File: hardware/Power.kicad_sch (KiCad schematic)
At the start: 40 parts, among them U2 LM2596S-12, U3 LM2596S-5, U4 LP2950-3.3_TO92

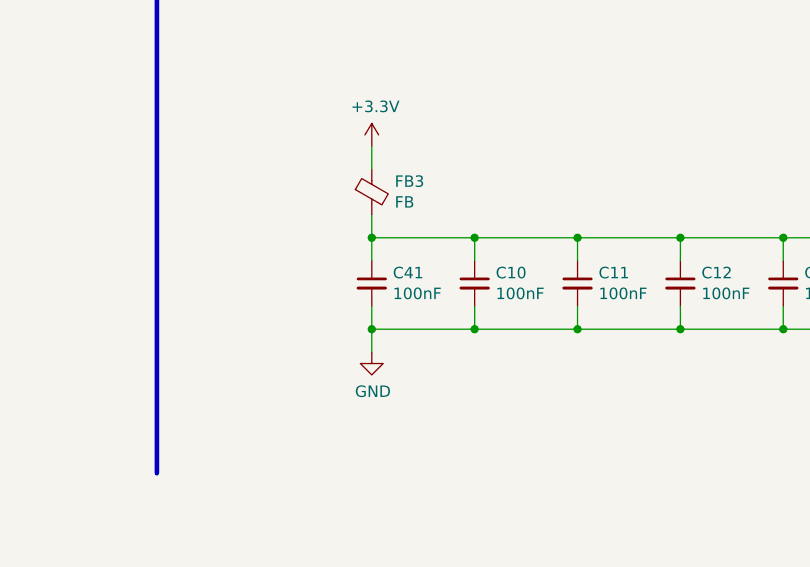
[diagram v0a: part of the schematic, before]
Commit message: changed clock and 5v converter coils, footprints rearrange commponets to fit the need now the board connector is vertical not horizontal relative to the pcb's longest side
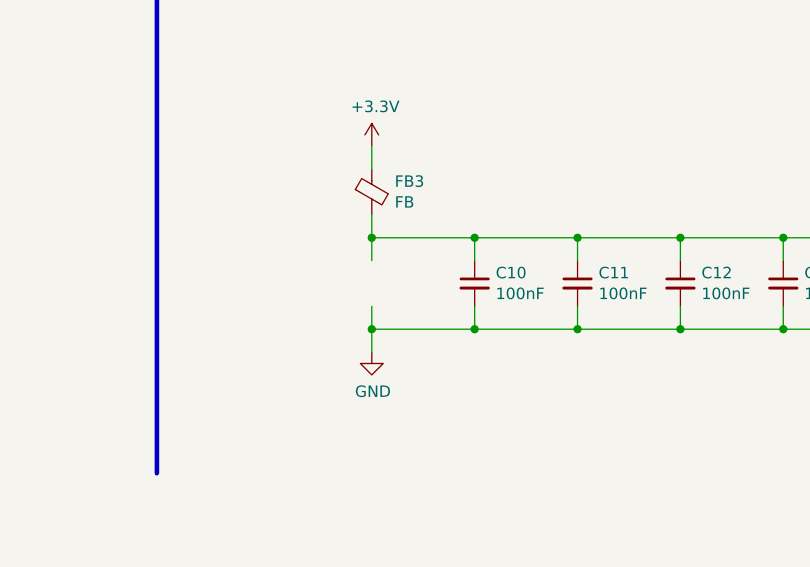
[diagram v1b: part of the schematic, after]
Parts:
- removed C41: 100nF, Capacitor_SMD:C_0603_1608Metric, symbol Device:C_Small
- L2, L4: footprint Inductor_SMD:L_12x12mm_H8mm -> Inductor_SMD:L_7.3x7.3_H4.5
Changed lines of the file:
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@@
     (property "Reference" "L4" (id 0) (at 59.69 148.844 90))
     (property "Value" "22uH" (id 1) (at 59.69 152.654 90))
-    (property "Footprint" "Inductor_SMD:L_12x12mm_H8mm" (id 2) (at 59.69 151.384 0)
+    (property "Footprint" "Inductor_SMD:L_7.3x7.3_H4.5" (id 2) (at 59.69 151.384 0)
       (effects (font (size 1.27 1.27)) hide)
     )
@@
     (pin "5")
   )
-  (symbol (lib_id "Device:C_Small") (at 200.406 145.288 0) (unit 1)
-    (in_bom yes) (on_board yes)
-    (property "Reference" "C41" (id 0) (at 202.7428 144.1196 0)
-      (effects (font (size 1.27 1.27)) (justify left))
-    )
-    (property "Value" "100nF" (id 1) (at 202.7428 146.431 0)
-      (effects (font (size 1.27 1.27)) (justify left))
-    )
-    (property "Footprint" "Capacitor_SMD:C_0603_1608Metric" (id 2) (at 200.406 145.288 0)
-      (effects (font (size 1.27 1.27)) hide)
-    )
-    (property "Datasheet" "~" (id 3) (at 200.406 145.288 0)
-      (effects (font (size 1.27 1.27)) hide)
-    )
-    (pin "1")
-    (pin "2")
-  )
   (symbol (lib_id "Device:L_Small") (at 119.38 156.464 90) (unit 1)
     (in_bom yes) (on_board yes)
     (property "Reference" "L2" (id 0) (at 119.38 153.924 90))
     (property "Value" "22uH" (id 1) (at 119.38 157.734 90))
-    (property "Footprint" "Inductor_SMD:L_12x12mm_H8mm" (id 2) (at 119.38 156.464 0)
-      (effects (font (size 1.27 1.27)) hide)
-    )
+    (property "Footprint" "Inductor_SMD:L_7.3x7.3_H4.5" (id 2) (at 119.38 156.464 0)
+      (effects (font (size 1.27 1.27)) hide)
+    )

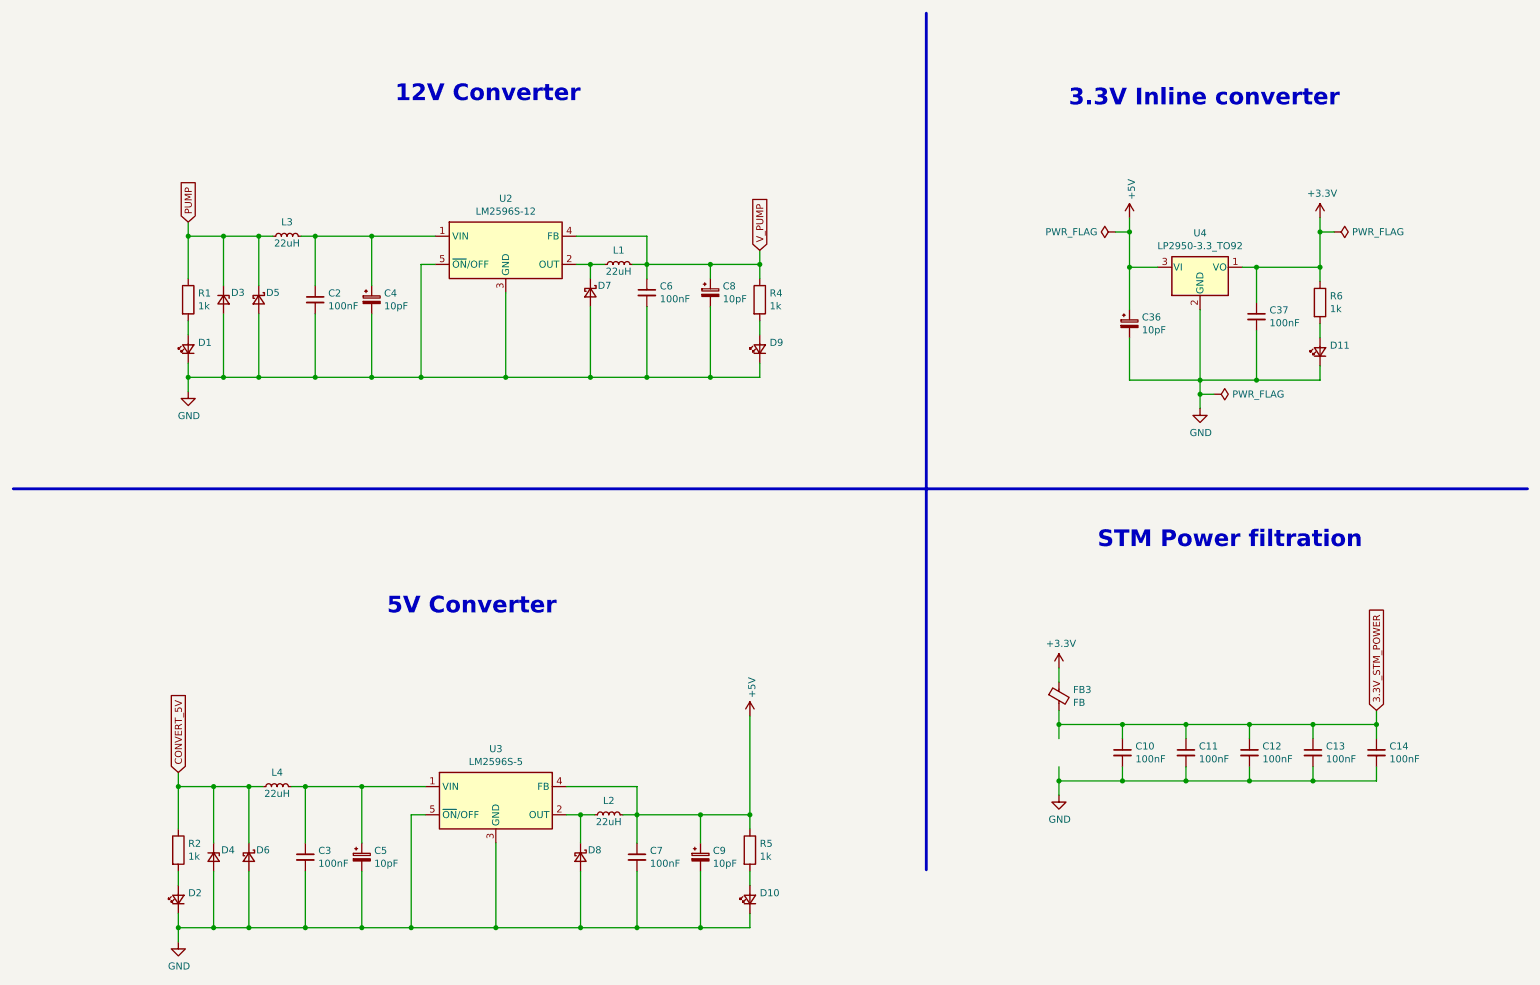
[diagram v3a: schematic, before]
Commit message: major schematic update, changed optocouplers for different, added new fuses for 5v supply for water and potentiometers and 24v supply for BSPD/ESB, updated autosport connector, and some other changes
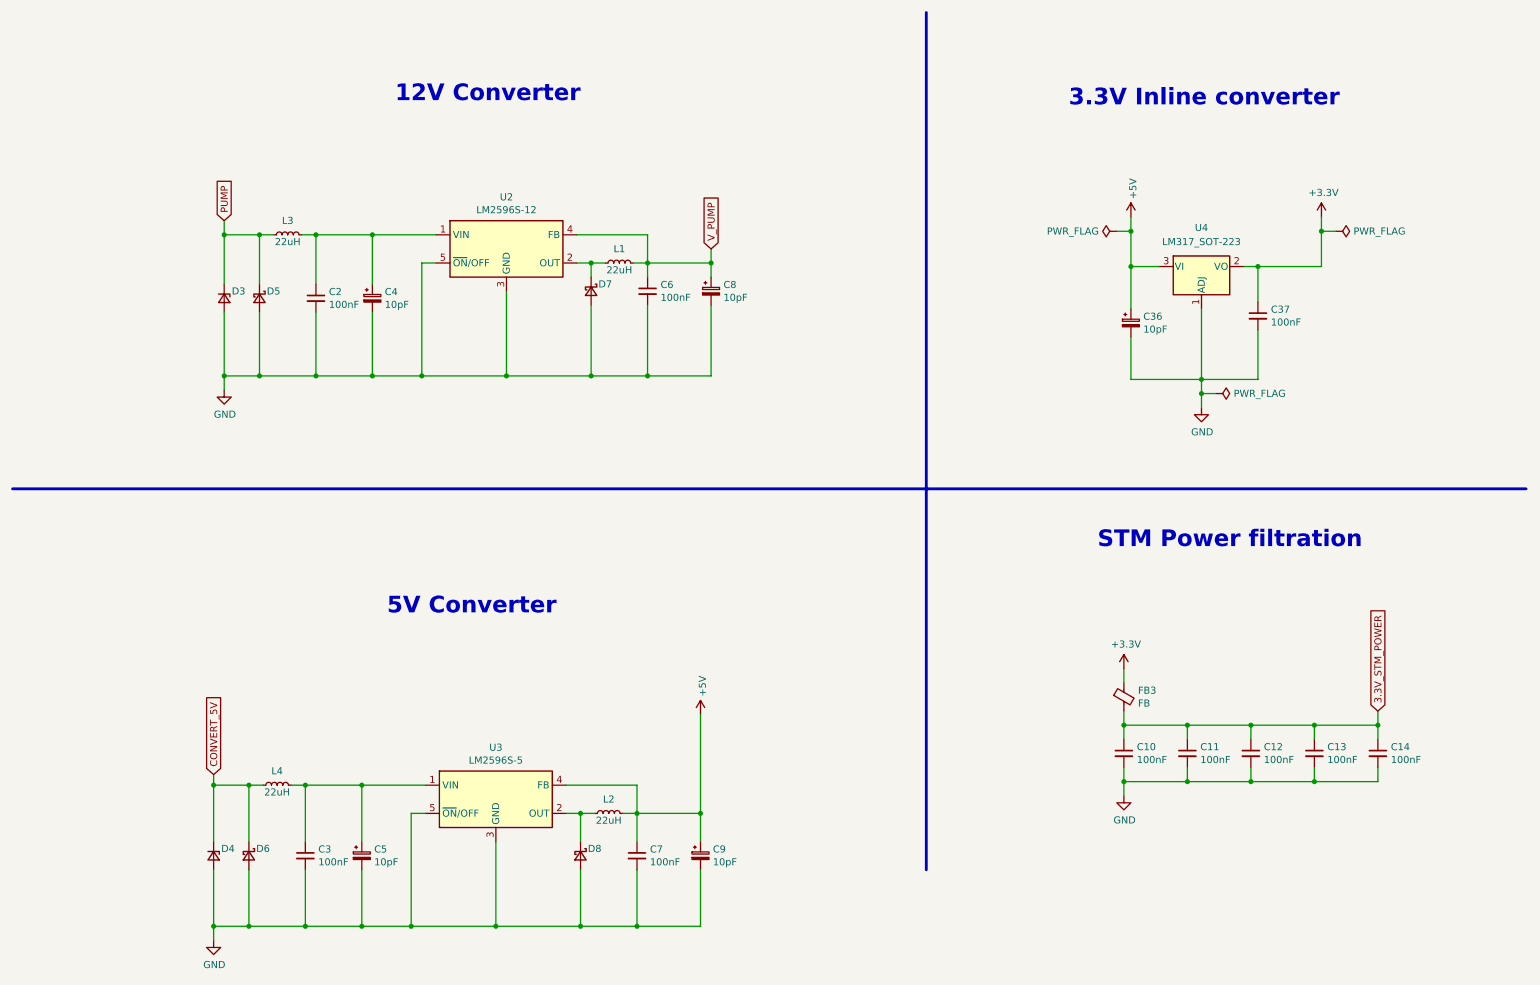
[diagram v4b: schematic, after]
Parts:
- removed D1, D2: IN, Diode_SMD:D_0603_1608Metric, symbol Device:LED_Small
- removed D10, D11, D9: OUT, Diode_SMD:D_0603_1608Metric, symbol Device:LED_Small
- removed R1, R2, R4, R5, R6: 1k, Resistor_SMD:R_0603_1608Metric, symbol Device:R
- removed U4: LP2950-3.3_TO92, Package_TO_SOT_SMD:SOT-223-3_TabPin2, symbol Regulator_Linear:LP2950-3.3_TO92
- added U4: LM317_SOT-223, Package_TO_SOT_SMD:SOT-223-3_TabPin2, symbol Regulator_Linear:LM317_SOT-223
- L1, L3: footprint Inductor_SMD:L_12x12mm_H8mm -> Inductor_SMD:L_7.3x7.3_H3.5
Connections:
- net +3V3: now also U4.2 (VO)
- net +5V: now also U4.3 (VI)
- net GND: now also U4.1 (ADJ)
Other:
- moved on the sheet: FB3

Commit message: changed some footprints for clarity, and made some progress on board
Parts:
- added L5: L_Small, symbol Device:L_Small
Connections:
- net 3.3V_STM_POWER: now also L5.2; no longer C10.1
- net GND: now also C10.1; no longer C10.2
- net CONVERT_5V renamed 5V_CONVERT_24V
- net PUMP renamed PUMP_24V
- net V_PUMP renamed PUMP_12V
- new net 3.3V_STM_REF+: C10.2, L5.1
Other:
- moved on the sheet: FB3

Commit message: finished new wersion of the board
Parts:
- L5: footprint (none) -> Inductor_SMD:L_0603_1608Metric
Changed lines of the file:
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@@
     (property "Reference" "L5" (id 0) (at 217.805 135.255 90))
     (property "Value" "L_Small" (id 1) (at 217.805 137.795 90))
-    (property "Footprint" "" (id 2) (at 217.805 140.335 0)
+    (property "Footprint" "Inductor_SMD:L_0603_1608Metric" (id 2) (at 217.805 140.335 0)
       (effects (font (size 1.27 1.27)) hide)
     )
